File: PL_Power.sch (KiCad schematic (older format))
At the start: 37 parts, among them U30 MPM3840GQV-Z, U31 MPM3840GQV-Z, U32 MPM3810AGQB-Z, U33 MPM3840GQV-Z

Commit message: Pre-Production Push
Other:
- note added: "Page 15/18 of datasheet\nR1 = 200K,\nR2 = R1/((Vout/0.6)-1) = 100k"
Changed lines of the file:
@@
 $Descr A3 16535 11693
 encoding utf-8
-Sheet 13 20
+Sheet 12 20
 Title "PL Power Kria"
 Date "2022-01-04"
@@
 Wire Wire Line
 	12150 8700 12150 9100
+Text Notes 6210 6900 0    50   ~ 0
+Page 15/18 of datasheet\nR1 = 200K,\nR2 = R1/((Vout/0.6)-1) = 100k
 $EndSCHEMATC

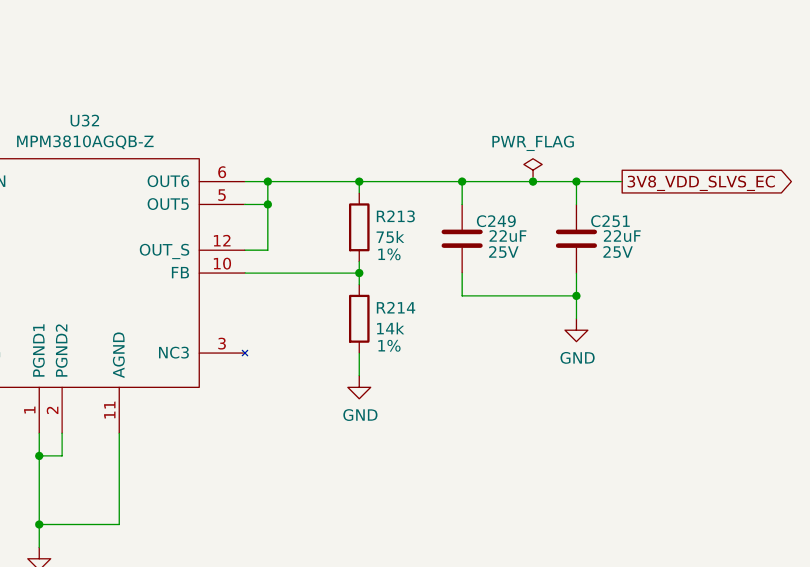
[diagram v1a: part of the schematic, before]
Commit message: Update to Kicad 7
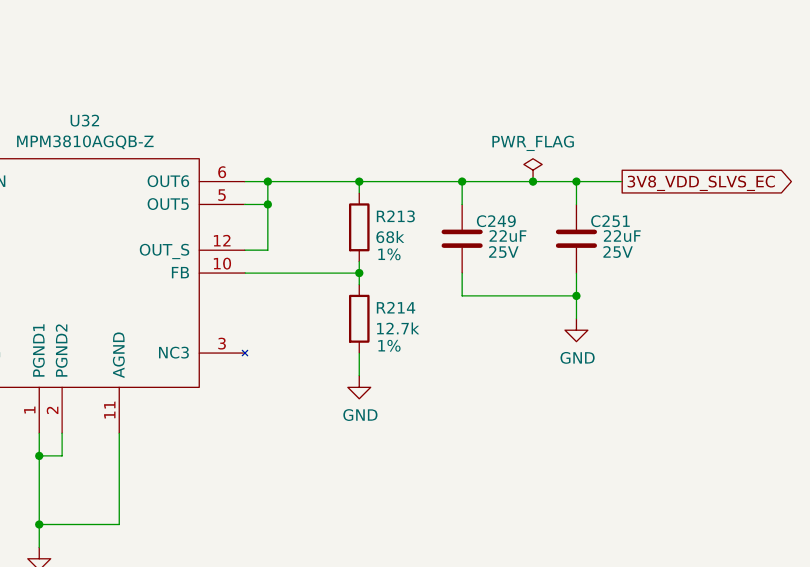
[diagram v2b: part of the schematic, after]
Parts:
- R213: value 75k -> 68k; PartNumber CRCW040275K0FKEDC -> RMCF0402FT68K0
- R214: value 14k -> 12.7k; PartNumber ERJ-2RKF1302X -> ERJ-2RKF1272X
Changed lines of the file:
@@
 AR Path="/616D3766/62C1F592" Ref="R213"  Part="1"
 F 0 "R213" H 13270 7846 50  0000 L CNN
-F 1 "75k" H 13270 7755 50  0000 L CNN
+F 1 "68k" H 13270 7755 50  0000 L CNN
 F 2 "Resistor_SMD:R_0402_1005Metric" V 13130 7800 50  0001 C CNN
 F 3 "~" H 13200 7800 50  0001 C CNN
-F 4 "CRCW040275K0FKEDC" H 13200 7800 50  0001 C CNN "PartNumber"
+F 4 "RMCF0402FT68K0" H 13200 7800 50  0001 C CNN "PartNumber"
 F 5 "1%" H 13330 7680 50  0000 C CNN "Tol"
 F 6 "1/16W" H 13200 7800 50  0001 C CNN "Power"
@@
 AR Path="/616D3766/634530C1" Ref="R214"  Part="1"
 F 0 "R214" H 13270 8246 50  0000 L CNN
-F 1 "14k" H 13270 8155 50  0000 L CNN
+F 1 "12.7k" H 13270 8155 50  0000 L CNN
 F 2 "Resistor_SMD:R_0402_1005Metric" V 13130 8200 50  0001 C CNN
 F 3 "~" H 13200 8200 50  0001 C CNN
-F 4 "ERJ-2RKF1302X" H 13200 8200 50  0001 C CNN "PartNumber"
+F 4 "ERJ-2RKF1272X" H 13200 8200 50  0001 C CNN "PartNumber"
 F 5 "1%" H 13330 8080 50  0000 C CNN "Tol"
 F 6 "1/10W" H 13200 8200 50  0001 C CNN "Power"
